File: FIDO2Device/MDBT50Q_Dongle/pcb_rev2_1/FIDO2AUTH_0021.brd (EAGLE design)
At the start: 19.1 x 31.8 mm, 36 parts, among them CN1 TE-1734028, CN2 IF_4PIN, SW1 SKRPACE010, SW2 SKTADAE010, U1 MDBT50Q-P1M, U2 XC6206P332MR-G, U3 ATECC608A-MAHDA-S, X1 NX3215SA-32.768K

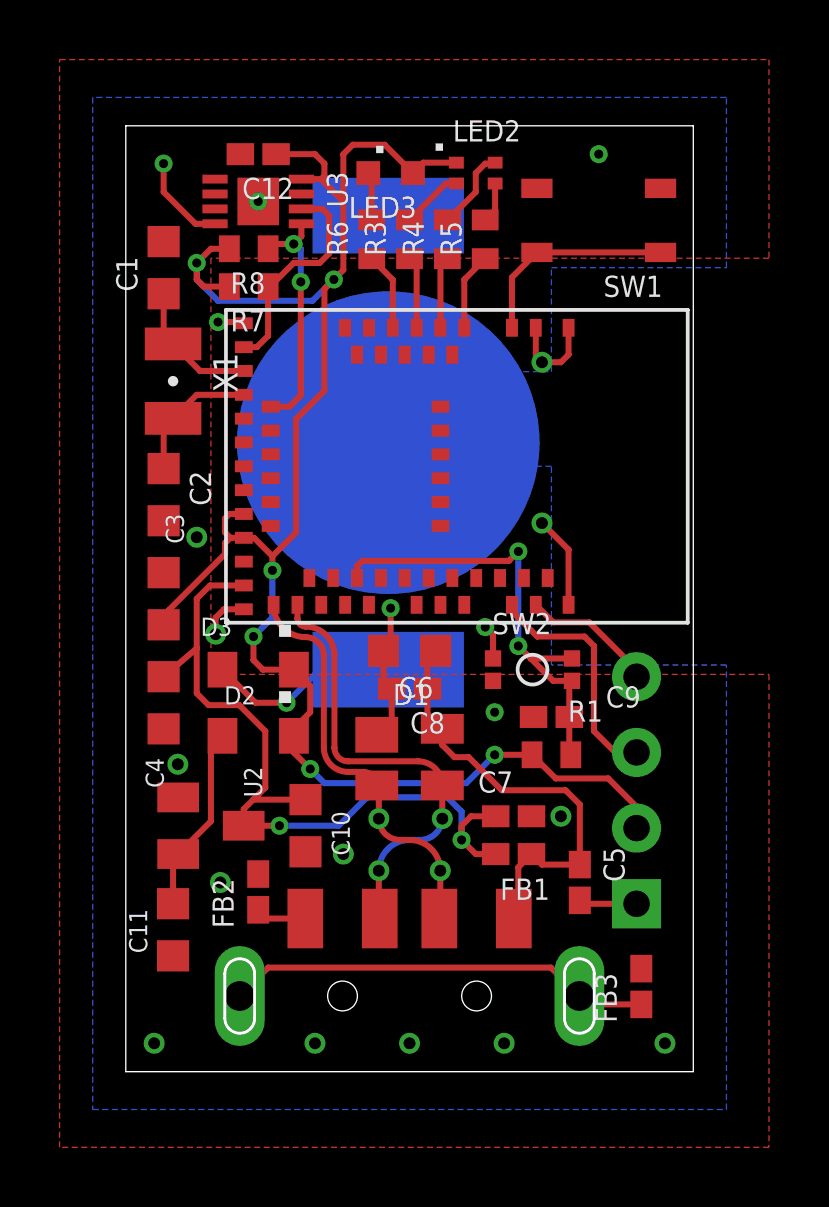
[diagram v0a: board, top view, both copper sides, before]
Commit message: リファクタリング
・RESET配線のビア経由部分を修正（折り返しをつける）
・D_N配線の不要なビアを削除
・ベタグラウンドパターンを整備（通りを良くする）
・カソードマークの位置を修正
・ビアの位置を修正
・ビアの小穴化
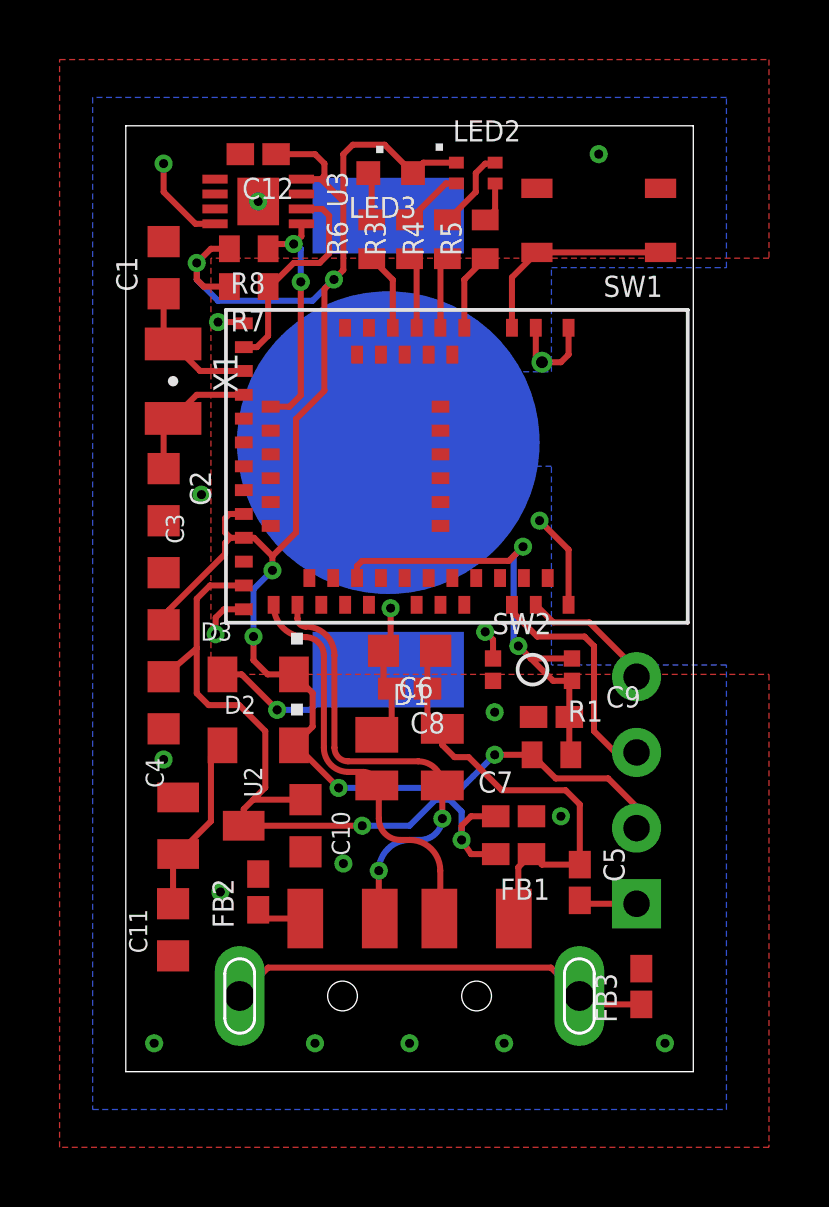
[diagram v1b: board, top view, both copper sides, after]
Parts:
- moved D2 0.32 mm to (4.45, 11.0)
- moved D3 0.16 mm to (4.45, 13.3)
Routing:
- net RESET: track 15.4 -> 16.0 mm
- net D_N: vias 2 -> 0

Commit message: 配線データを修正
・セキュアICのVDD配線を基板背面で行うよう修正
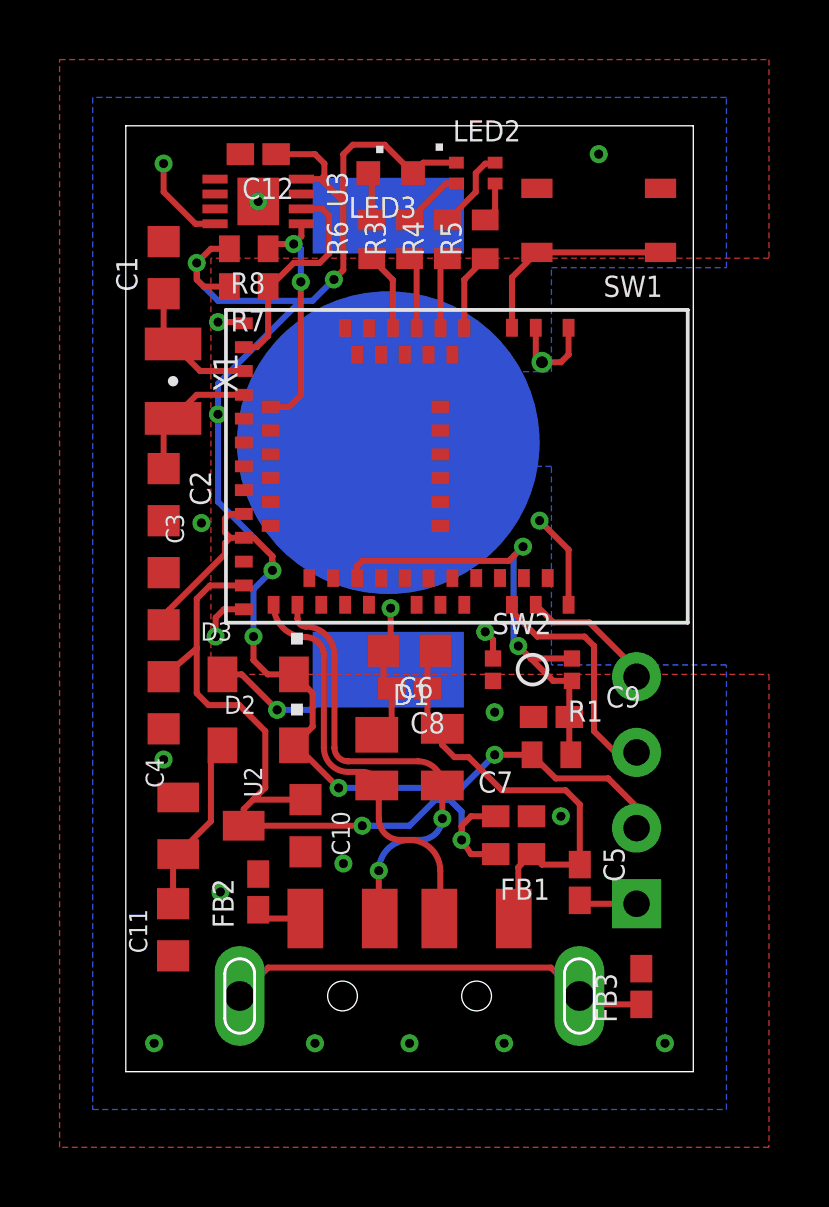
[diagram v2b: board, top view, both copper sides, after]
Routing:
- net VDD_NRF: track 61.3 -> 62.1 mm, vias 6 -> 7
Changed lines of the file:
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@@
 <wire x1="3.9625" y1="15.52" x2="3.29625" y2="15.52" width="0.2032" layer="1"/>
 <wire x1="3.29625" y1="15.52" x2="3.01625" y2="15.24" width="0.2032" layer="1"/>
-<wire x1="3.01625" y1="15.24" x2="3.01625" y2="14.684375" width="0.2032" layer="1"/>
+<wire x1="3.01625" y1="15.24" x2="3.01625" y2="14.605" width="0.2032" layer="1"/>
 <wire x1="8.65" y1="14.12875" x2="8.65" y2="13.13375" width="0.2032" layer="1"/>
 <wire x1="8.65" y1="13.13375" x2="8.925" y2="12.85875" width="0.2032" layer="1"/>
@@
 <via x="3.175" y="6.0325" extent="1-16" drill="0.3048"/>
 <via x="1.27" y="10.4775" extent="1-16" drill="0.3048"/>
-<via x="3.01625" y="14.684375" extent="1-16" drill="0.3048"/>
+<via x="3.01625" y="14.605" extent="1-16" drill="0.3048"/>
 <via x="7.3025" y="6.985" extent="1-16" drill="0.3048"/>
-<via x="2.54" y="19.3675" extent="1-16" drill="0.3048"/>
+<via x="2.54" y="18.415" extent="1-16" drill="0.3048"/>
 <via x="0.9525" y="0.9525" extent="1-16" drill="0.3048"/>
 <via x="6.35" y="0.9525" extent="1-16" drill="0.3048"/>
@@
 <wire x1="13.6375" y1="10.63625" x2="14.43125" y2="9.8425" width="0.2032" layer="1"/>
 <via x="7.14375" y="9.525" extent="1-16" drill="0.3048"/>
-<wire x1="12.3825" y1="10.63625" x2="11.668125" y2="9.921875" width="0.2032" layer="16"/>
-<wire x1="11.668125" y1="9.921875" x2="11.43" y2="9.68375" width="0.2032" layer="16"/>
+<wire x1="12.3825" y1="10.63625" x2="11.27125" y2="9.525" width="0.2032" layer="16"/>
 <wire x1="4.28625" y1="13.81125" x2="4.28625" y2="14.605" width="0.2032" layer="1"/>
 <wire x1="1.27" y1="15" x2="1.42875" y2="15.478125" width="0.2032" layer="1"/>
@@
 <wire x1="8.6875" y1="31.115" x2="9.64" y2="30.1625" width="0.2032" layer="1"/>
 <wire x1="13.6375" y1="10.63625" x2="12.3825" y2="10.63625" width="0.2032" layer="1"/>
-<wire x1="4.92125" y1="17.30375" x2="5.715" y2="18.0975" width="0.2032" layer="1"/>
-<wire x1="5.715" y1="18.0975" x2="5.715" y2="21.9075" width="0.2032" layer="1"/>
-<wire x1="5.715" y1="21.9075" x2="6.6675" y2="22.86" width="0.2032" layer="1"/>
-<wire x1="6.6675" y1="22.86" x2="6.6675" y2="26.273125" width="0.2032" layer="1"/>
 <wire x1="7.3025" y1="29.21" x2="7.3025" y2="30.7975" width="0.2032" layer="1"/>
 <wire x1="7.3025" y1="30.7975" x2="7.62" y2="31.115" width="0.2032" layer="1"/>
@@
 <wire x1="6.6675" y1="30.48" x2="6.6675" y2="30.075" width="0.2032" layer="1"/>
 <wire x1="6.6675" y1="30.075" x2="6.5525" y2="29.96" width="0.2032" layer="1"/>
-<wire x1="3.095625" y1="25.87625" x2="6.270625" y2="25.87625" width="0.2032" layer="16"/>
+<wire x1="3.095625" y1="25.87625" x2="5.794375" y2="25.87625" width="0.2032" layer="16"/>
+<wire x1="5.794375" y1="25.87625" x2="6.270625" y2="25.87625" width="0.2032" layer="16"/>
 <wire x1="6.270625" y1="25.87625" x2="6.985" y2="26.590625" width="0.2032" layer="16"/>
-<wire x1="6.6675" y1="26.273125" x2="6.985" y2="26.590625" width="0.2032" layer="1"/>
 <wire x1="7.3025" y1="29.21" x2="7.3025" y2="26.908125" width="0.2032" layer="1"/>
 <wire x1="7.3025" y1="26.908125" x2="6.985" y2="26.590625" width="0.2032" layer="1"/>
@@
 <wire x1="4.28625" y1="16.1925" x2="4.92125" y2="16.8275" width="0.2032" layer="16"/>
 <wire x1="7.14375" y1="9.525" x2="11.27125" y2="9.525" width="0.2032" layer="16"/>
-<wire x1="11.27125" y1="9.525" x2="11.43" y2="9.68375" width="0.2032" layer="16"/>
+<via x="3.095625" y="22.06625" extent="1-16" drill="0.3048"/>
+<wire x1="3.095625" y1="22.06625" x2="3.095625" y2="23.098125" width="0.2032" layer="16"/>
+<wire x1="3.095625" y1="23.098125" x2="5.794375" y2="25.796875" width="0.2032" layer="16"/>
+<wire x1="5.794375" y1="25.796875" x2="5.794375" y2="25.87625" width="0.2032" layer="16"/>
+<wire x1="3.095625" y1="22.06625" x2="3.095625" y2="19.129375" width="0.2032" layer="16"/>
+<wire x1="3.095625" y1="19.129375" x2="4.92125" y2="17.30375" width="0.2032" layer="16"/>
+<wire x1="4.92125" y1="17.30375" x2="4.92125" y2="16.8275" width="0.2032" layer="16"/>
 </signal>
 <signal name="VBUS">

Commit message: 部品データを修正
・セキュアIC、ESDに極性マークがついていなかったので追加
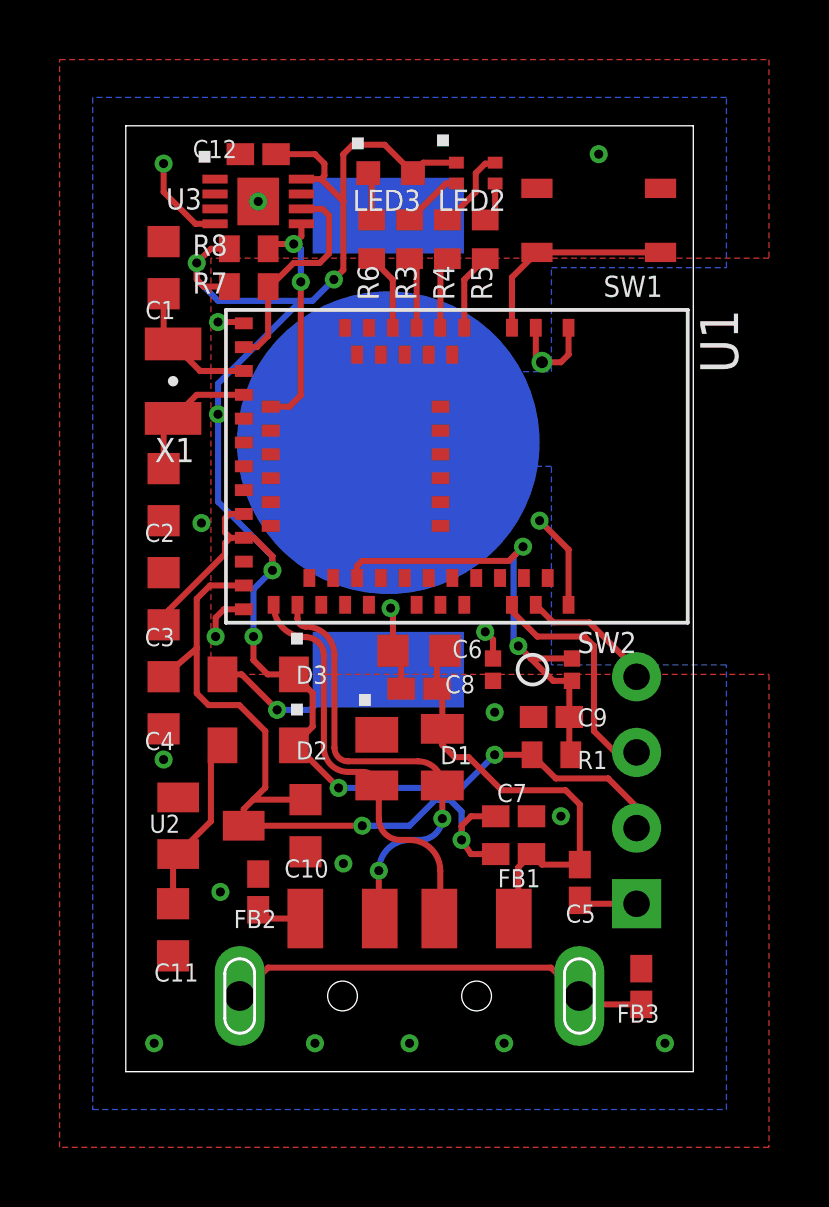
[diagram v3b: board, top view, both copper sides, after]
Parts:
- moved C6 0.32 mm to (9.84, 14.1)
- moved C8 0.32 mm to (9.84, 12.9)
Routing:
- net 0V: track 19.7 -> 17.9 mm

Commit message: プリント基板データを修正
・部品番号の印字イメージが抜けていたので、正しくプリント基板に反映されるよう修正
・DRC結果はエラー無し
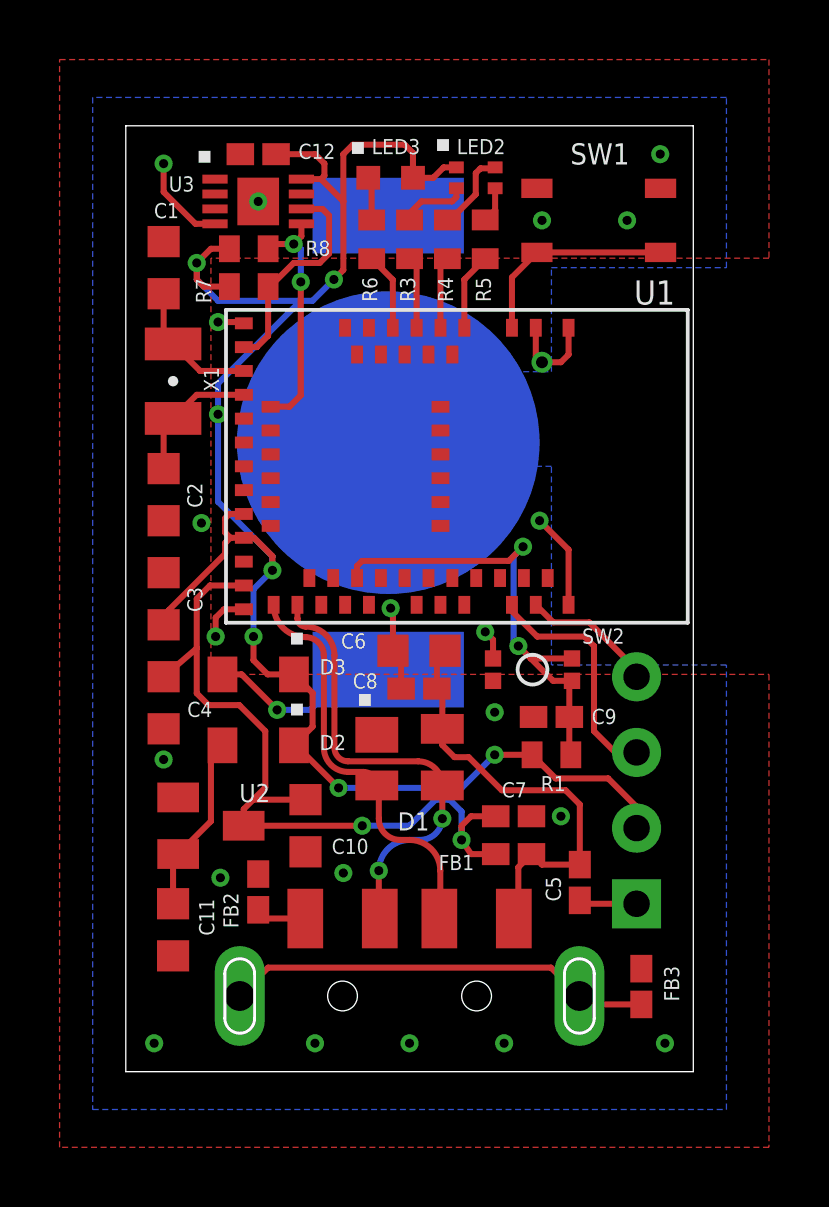
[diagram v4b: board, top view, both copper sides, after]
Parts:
- moved LED2 0.16 mm to (11.7, 30.0)
- moved LED3 0.16 mm to (8.89, 30.0)
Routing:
- net VDD_NRF: track 62.1 -> 62.6 mm
- net 0V: vias 20 -> 22
